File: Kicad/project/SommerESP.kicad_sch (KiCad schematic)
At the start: 36 parts, among them J1 Serial programmer, J2 BRIDGE CONEX, J3 SOMMER CONEX BOARD, J4 SOMMER CONEX KEYPAD, J5 BRIDGE POWER, J6 SOMMER OUTPUT OC, Q1 STN3NF06, U2 G3VM-61D1, U3 G3VM-61D1, U4 LM2596SX-3.3/NOPB, U5 ESP32-C3-WROOM-02

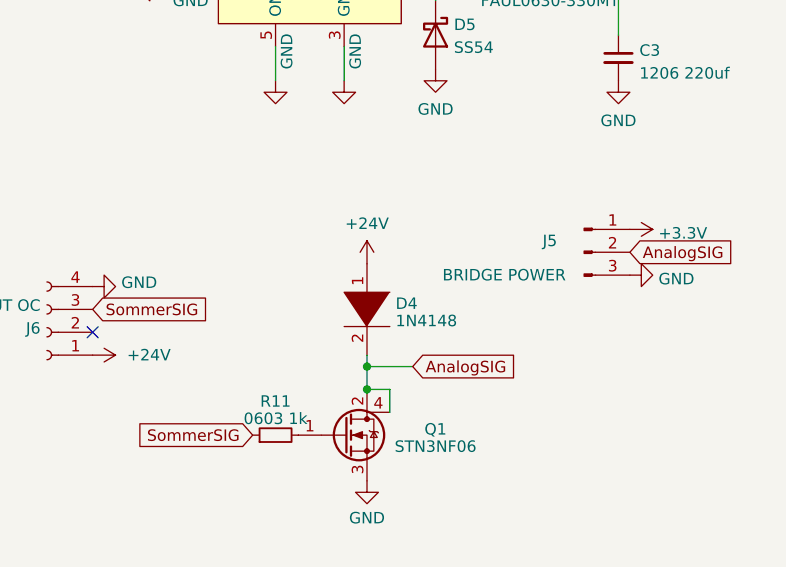
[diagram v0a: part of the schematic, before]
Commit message: Found an error in the schematic for Diode D4. Was inverted in the schematic but correct in the PCB and Photos.
Thank you to Stefano Gnocato for pointing that out!
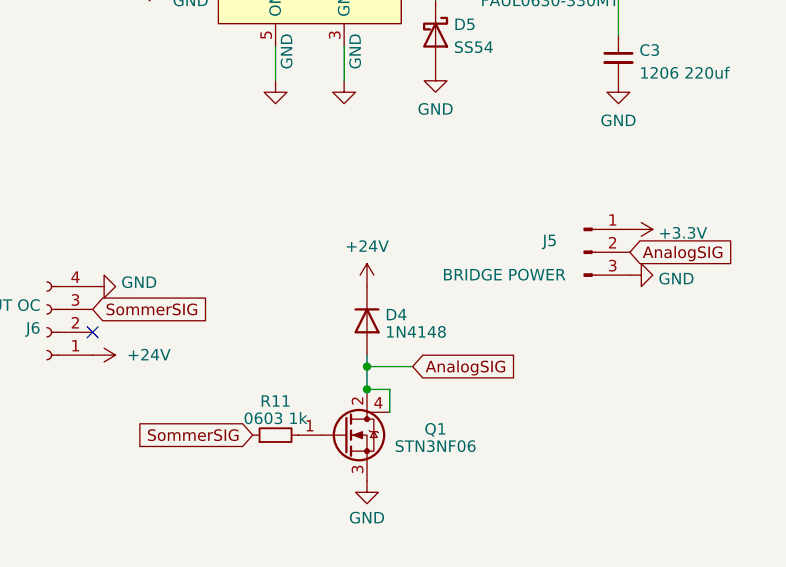
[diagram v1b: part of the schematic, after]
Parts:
- removed D4: 1N4148, Diode_THT:D_DO-35_SOD27_P7.62mm_Horizontal, symbol pspice:DIODE
- added D4: 1N4148, Diode_THT:D_DO-35_SOD27_P7.62mm_Horizontal, symbol Diode:1N4148
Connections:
- net +24V: now also D4.1 (K)
- net AnalogSIG: now also D4.2 (A)
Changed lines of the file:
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@@
     )
   )
-  (symbol (lib_id "power:+24V") (at 236.22 64.77 0) (unit 1)
-    (in_bom yes) (on_board yes) (dnp no) (fields_autoplaced)
-    (property "Reference" "#PWR014" (at 236.22 68.58 0)
-      (effects (font (size 1.27 1.27)) hide)
-    )
-    (property "Value" "+24V" (at 236.22 60.3266 0)
-      (effects (font (size 1.27 1.27)))
-    )
-    (property "Footprint" "" (at 236.22 64.77 0)
-      (effects (font (size 1.27 1.27)) hide)
-    )
-    (property "Datasheet" "" (at 236.22 64.77 0)
+  (symbol (lib_id "power:+24V") (at 236.22 67.31 0) (unit 1)
+    (in_bom yes) (on_board yes) (dnp no) (fields_autoplaced)
+    (property "Reference" "#PWR014" (at 236.22 71.12 0)
+      (effects (font (size 1.27 1.27)) hide)
+    )
+    (property "Value" "+24V" (at 236.22 62.8666 0)
+      (effects (font (size 1.27 1.27)))
+    )
+    (property "Footprint" "" (at 236.22 67.31 0)
+      (effects (font (size 1.27 1.27)) hide)
+    )
+    (property "Datasheet" "" (at 236.22 67.31 0)
       (effects (font (size 1.27 1.27)) hide)
     )
@@
     )
   )
-  (symbol (lib_id "pspice:DIODE") (at 236.22 69.85 270) (unit 1)
-    (in_bom yes) (on_board yes) (dnp no) (fields_autoplaced)
-    (property "Reference" "D4" (at 239.395 69.2063 90)
-      (effects (font (size 1.27 1.27)) (justify left))
-    )
-    (property "Value" "1N4148" (at 239.395 71.1273 90)
-      (effects (font (size 1.27 1.27)) (justify left))
-    )
-    (property "Footprint" "Diode_THT:D_DO-35_SOD27_P7.62mm_Horizontal" (at 236.22 69.85 0)
-      (effects (font (size 1.27 1.27)) hide)
-    )
-    (property "Datasheet" "~" (at 236.22 69.85 0)
-      (effects (font (size 1.27 1.27)) hide)
-    )
-    (pin "1")
-    (pin "2")
-    (instances
-      (project "SommerESP"
-        (path "/fdfaab82-b631-42c7-9b66-01e568778cad"
-          (reference "D4") (unit 1)
-        )
-      )
-    )
-  )
   (symbol (lib_id "Connector:Conn_01x06_Pin") (at 148.59 91.44 180) (unit 1)
     (in_bom yes) (on_board yes) (dnp no) (fields_autoplaced)
@@
         )
       )
+    )
+  )
+  (symbol (lib_id "Diode:1N4148") (at 236.22 71.12 270) (unit 1)
+    (in_bom yes) (on_board yes) (dnp no) (fields_autoplaced)
+    (property "Reference" "D4" (at 238.252 70.4763 90)
+      (effects (font (size 1.27 1.27)) (justify left))
+    )
+    (property "Value" "1N4148" (at 238.252 72.3973 90)
+      (effects (font (size 1.27 1.27)) (justify left))
+    )
+    (property "Footprint" "Diode_THT:D_DO-35_SOD27_P7.62mm_Horizontal" (at 236.22 71.12 0)
+      (effects (font (size 1.27 1.27)) hide)
+    )
+    (property "Datasheet" "https://assets.nexperia.com/documents/data-sheet/1N4148_1N4448.pdf" (at 236.22 71.12 0)
+      (effects (font (size 1.27 1.27)) hide)
+    )
+    (property "Sim.Device" "D" (at 236.22 71.12 0)
+      (effects (font (size 1.27 1.27)) hide)
+    )
+    (property "Sim.Pins" "1=K 2=A" (at 236.22 71.12 0)
+      (effects (font (size 1.27 1.27)) hide)
+    )
+    (pin "1")
+    (pin "2")
+    (instances
+      (project "SommerESP"
+        (path "/fdfaab82-b631-42c7-9b66-01e568778cad"
+          (reference "D4") (unit 1)
+        )
+      )

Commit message: Updated Kicad to version 8 Added references to LCSC part numbers in the project and BOM Cleaned up a bit of silkscreen text and added some references Added JLCJLCJLCJLC on the silkscreen for the order number on JLC
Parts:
- C1, C2: LCSC (none) -> C501857
- C3, C4: LCSC (none) -> C412252
- D1: LCSC (none) -> C397047
- D2: LCSC (none) -> C497961
- D3: LCSC (none) -> C5449114
- D4: LCSC (none) -> C402212
- D5: LCSC (none) -> C2902914
- J1: LCSC (none) -> C37208
- J2, J5: LCSC (none) -> C144394
- J3: LCSC (none) -> C146243
- J4: LCSC (none) -> C49257
- J6: LCSC (none) -> C2718488
- L1: LCSC (none) -> C7461364
- Q1: LCSC (none) -> C222218
- R1, R10, R2, R9: LCSC (none) -> C3017758
- R11, R7, R8: LCSC (none) -> C116692
- R12, R13, R3, R4: LCSC (none) -> C2930027
- R5, R6: LCSC (none) -> C2907159
- S1, S2: LCSC (none) -> C2905192
- U2, U3: LCSC (none) -> C469131
- U4: symbol LM2596SX-3.3 NOPB:LM2596SX-3.3/NOPB -> LM2596SX-3.3 NOPB:LM2596SX-3.3/NOPB; LCSC (none) -> C5186052
- U5: LCSC (none) -> C2934560

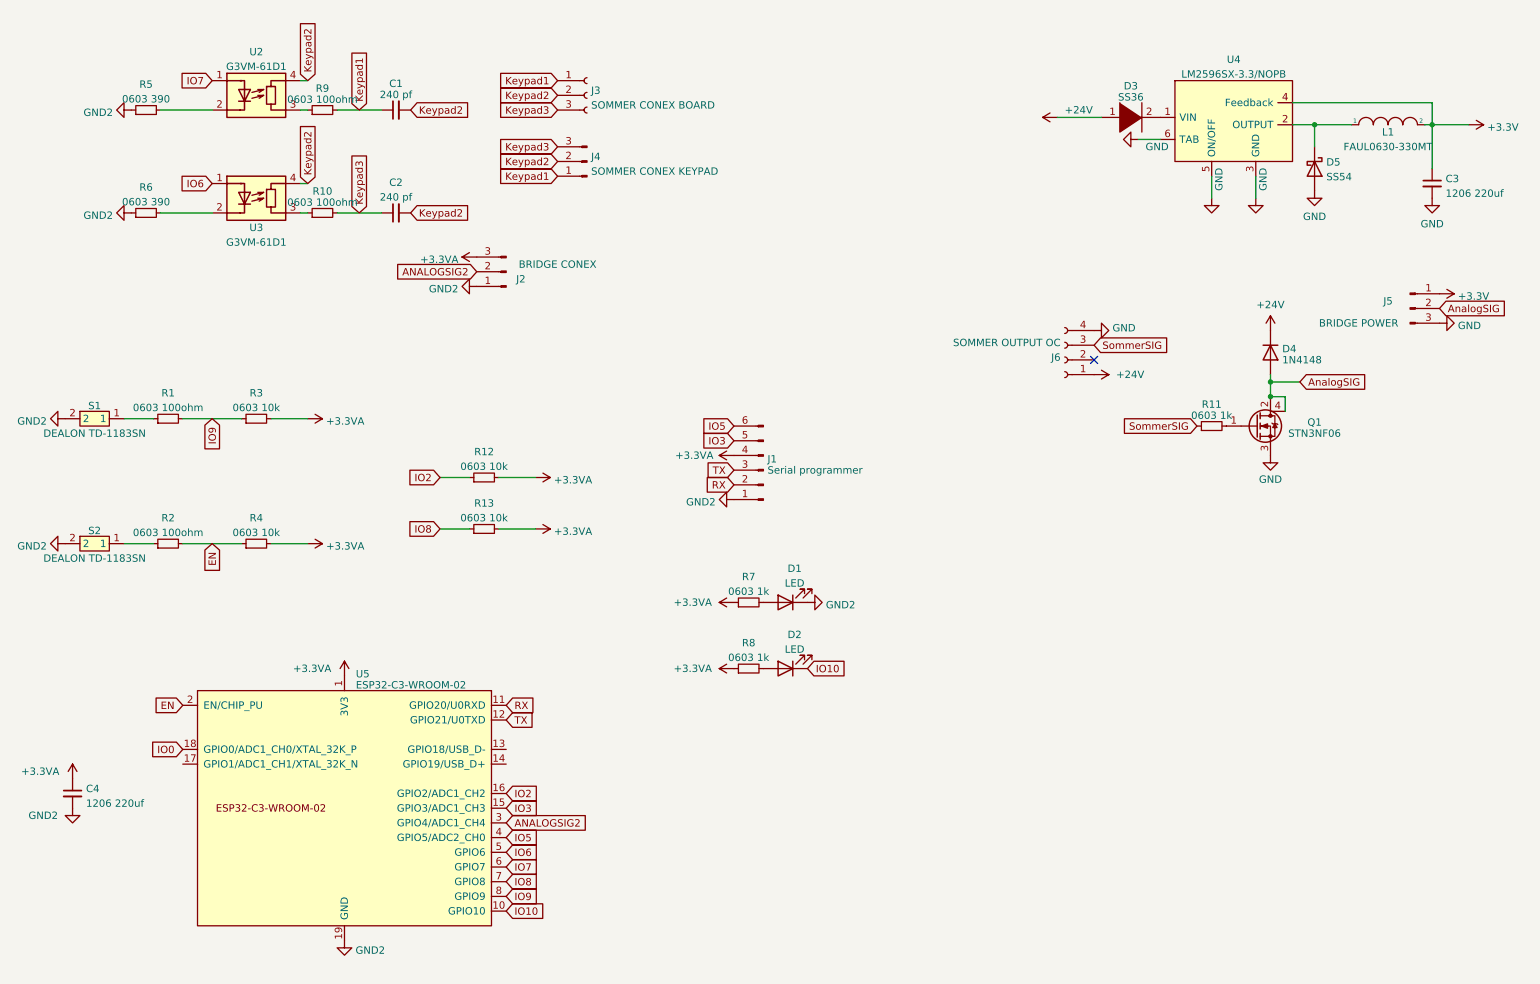
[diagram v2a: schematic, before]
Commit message: Updated to V2. This is a transition version.
Updated yaml and added M3c4tr0x confirmation of
board working
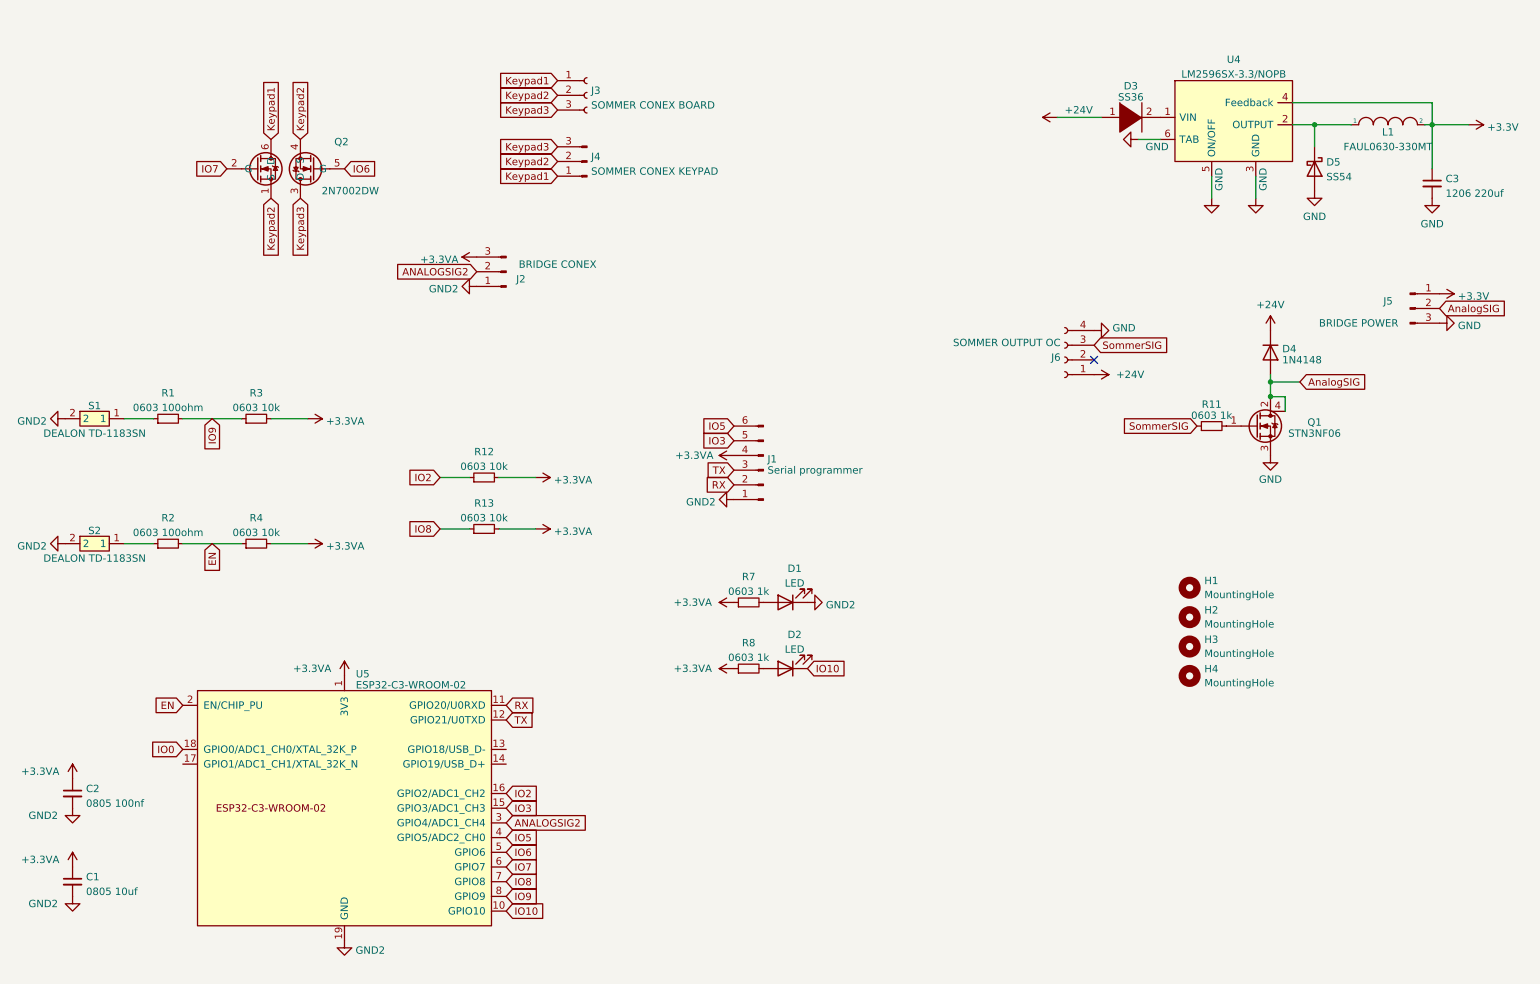
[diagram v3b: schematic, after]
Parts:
- removed C2: 240 pf, Capacitor_SMD:C_0805_2012Metric_Pad1.18x1.45mm_HandSolder, symbol Device:C_Small
- removed R10, R9: 0603 100ohm, Resistor_SMD:R_0603_1608Metric_Pad0.98x0.95mm_HandSolder, symbol Device:R_Small
- removed R5, R6: 0603 390, Resistor_SMD:R_0603_1608Metric_Pad0.98x0.95mm_HandSolder, symbol Device:R_Small
- removed U2, U3: G3VM-61D1, CustomLibrary:G3VM-61D1, symbol Isolator:NSL-32
- added H1, H2, H3, H4: MountingHole, CustomLibrary:Panelizing_1_1, symbol Mechanical:MountingHole
- added Q2: 2N7002DW, Package_TO_SOT_SMD:SOT-363_SC-70-6, symbol Custom:2N7002DW
- C1: value 240 pf -> 0805 10uf; LCSC C501857 -> C412252
- C2: renamed from C4; value 1206 220uf -> 0805 100nf; footprint Capacitor_SMD:C_1206_3216Metric_Pad1.33x1.80mm_HandSolder -> Capacitor_SMD:C_0805_2012Metric_Pad1.18x1.45mm_HandSolder
- D4: footprint Diode_THT:D_DO-35_SOD27_P7.62mm_Horizontal -> Diode_SMD:D_SOD-123
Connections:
- net +3.3VA: now also C1.1
- net GND2: now also C1.2
- net IO6: now also Q2.5 (G)
- net IO7: now also Q2.2 (G)
- net Keypad1: now also Q2.6 (D); no longer C1.1
- net Keypad2: now also Q2.1 (S), Q2.4 (S); no longer C1.2
- net Keypad3: now also Q2.3 (D)

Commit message: Version 3.0 of SommerESP
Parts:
- removed H1, H2, H3, H4: MountingHole, CustomLibrary:Panelizing_1_1, symbol Mechanical:MountingHole
- removed J1: Serial programmer, Connector_PinHeader_2.54mm:PinHeader_1x06_P2.54mm_Vertical, symbol Connector:Conn_01x06_Pin
- removed J2: BRIDGE CONEX, Connector_JST:JST_XH_B3B-XH-A_1x03_P2.50mm_Vertical, symbol Connector:Conn_01x03_Male
- removed J5: BRIDGE POWER, Connector_JST:JST_XH_B3B-XH-A_1x03_P2.50mm_Vertical, symbol Connector:Conn_01x03_Male
- added C4: 0805 22uf, Capacitor_SMD:C_0805_2012Metric_Pad1.18x1.45mm_HandSolder, symbol Device:C_Small
- added J1: Serial programmer, Connector_PinHeader_2.54mm:PinHeader_1x08_P2.54mm_Vertical, symbol Connector:Conn_01x08_Pin
- U4: value LM2596SX-3.3/NOPB -> LM2596SX-3.3/NOPB
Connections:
- net +3.3VA is gone; now on net +3.3V: C1.1, C2.1, R12.2, R13.2, R3.2, R4.2, R7.1, R8.1, U5.1 (3V3)
- net ANALOGSIG2 is gone; now on net AnalogSIG: U5.3 (GPIO4/ADC1_CH4)
- net GND2 is gone; now on net GND: C1.2, C2.2, D1.1 (K), S1.2, S2.2, U5.19 (GND), U5.9 (GND)
- net +3.3V: now also J1.8 (Pin_8)
- net EN: now also C4.1
- net GND: now also C4.2, J1.1 (Pin_1)
- net IO3: now also J1.2 (Pin_2)
- net IO5: now also J1.7 (Pin_7)
- net RX: now also J1.6 (Pin_6)
- net TX: now also J1.5 (Pin_5)
- net IO18: now reaches U5.13 (GPIO18/USB_D-)
- net IO18: now also J1.4 (Pin_4)
- net IO19: now reaches U5.14 (GPIO19/USB_D+)
- net IO19: now also J1.3 (Pin_3)
